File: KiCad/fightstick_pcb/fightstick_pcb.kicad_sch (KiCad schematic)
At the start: 98 parts, among them J1 USB_B_Micro, J2 Conn_01x02, J3 Conn_02x18_Odd_Even, J4 Conn_02x18_Odd_Even, SW1 SW_Push, SW10 SW_Push, SW11 SW_Push, SW12 SW_Push, SW2 SW_Push, SW3 SW_Push, SW4 SW_Push, SW5 SW_Push, SW6 SW_Push, SW7 SW_Push, SW8 SW_Push, SW9 SW_Push, U1 NCP1117-3.3_SOT223, U10 SN74LVC1G14DBV, U11 SN74LVC1G14DBV, U12 SN74LVC1G14DBV, U13 SN74LVC1G14DBV, U14 SN74LVC1G14DBV, U15 SN74LVC1G14DBV, U2 W25Q128JVS, U3 RP2040, U4 SN74LVC1G14DBV, U5 SN74LVC1G14DBV, U6 SN74LVC1G14DBV, U7 SN74LVC1G14DBV, U8 SN74LVC1G14DBV, U9 SN74LVC1G14DBV, Y1 ABM8-272-T3

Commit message: Added LEDs and Reset
Added player leds, reset button and meaningfull pin names
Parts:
- added C30: 100n, symbol Device:C
- added D2, D3, D4, D5: GREEN, symbol Device:LED
- added R31: 10k, symbol Device:R
- added R32, R33, R34, R35: 1k, symbol Device:R
- added SW13: SW_Push, symbol Switch:SW_Push
- D1: value LED -> GREEN
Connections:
- net +3V3: now also R31.1
- net GND: now also C30.2, R32.2, R33.2, R34.2, R35.2, SW13.2
- net GPIO0: no longer U3.2 (GPIO0)
- net GPIO1: no longer U3.3 (GPIO1)
- net GPIO10: no longer U3.13 (GPIO10)
- net GPIO11: no longer U3.14 (GPIO11)
- net GPIO14: no longer U9.4
- net GPIO15: no longer U10.4
- net GPIO16: no longer U11.4
- net GPIO17: no longer U7.4
- net GPIO18: no longer U13.4, U3.29 (GPIO18)
- net GPIO19: no longer U15.4, U3.30 (GPIO19)
- net GPIO2: no longer U3.4 (GPIO2)
- net GPIO20: no longer U3.31 (GPIO20), U8.4
- net GPIO21: no longer U3.32 (GPIO21), U6.4
- net GPIO22: no longer U3.34 (GPIO22), U5.4
- net GPIO23: no longer U3.35 (GPIO23), U4.4
- net GPIO24: no longer U12.4, U3.36 (GPIO24)
- net GPIO25: no longer U14.4, U3.37 (GPIO25)
- net GPIO26_ADC0: no longer RV1.2, U3.38 (GPIO26_ADC0)
- net GPIO27_ADC1: no longer RV2.2, U3.39 (GPIO27_ADC1)
- net GPIO3: no longer U3.5 (GPIO3)
- net GPIO8: no longer U3.11 (GPIO8)
- net GPIO9: no longer U3.12 (GPIO9)
- net RUN: now also C30.1, R31.2, SW13.1
- new net: D5.1 (K), R35.1
- new net: D3.1 (K), R33.1
- new net: D2.1 (K), R32.1
- new net: D4.1 (K), R34.1
- new net BUTTON_0: U10.4, U3.12 (GPIO9)
- new net BUTTON_1: U3.11 (GPIO8), U9.4
- new net BUTTON_A: U14.4, U3.37 (GPIO25)
- new net BUTTON_B: U12.4, U3.36 (GPIO24)
- new net BUTTON_LB: U13.4, U3.29 (GPIO18)
- new net BUTTON_LT: U3.34 (GPIO22), U5.4
- new net BUTTON_RB: U15.4, U3.30 (GPIO19)
- new net BUTTON_RT: U3.35 (GPIO23), U4.4
- new net BUTTON_SELECT: U11.4, U3.13 (GPIO10)
- new net BUTTON_START: U3.14 (GPIO11), U7.4
- new net BUTTON_X: U3.32 (GPIO21), U6.4
- new net BUTTON_Y: U3.31 (GPIO20), U8.4
- new net JOYSTICK_0: RV1.2, U3.38 (GPIO26_ADC0)
- new net JOYSTICK_1: RV2.2, U3.39 (GPIO27_ADC1)
- new net PLAYER_LED_0: D5.2 (A), U3.2 (GPIO0)
- new net PLAYER_LED_1: D4.2 (A), U3.3 (GPIO1)
- new net PLAYER_LED_2: D3.2 (A), U3.4 (GPIO2)
- new net PLAYER_LED_3: D2.2 (A), U3.5 (GPIO3)
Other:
- note added: "Player leds"
- note added: "Reset button"
- moved on the sheet: C17, C18, C21, C26, C27, C28, C29, J3, J4, R13, R14, R23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

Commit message: Added connectors
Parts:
- removed D2, D3, D4, D5: GREEN, symbol Device:LED
- removed J3, J4: Conn_02x18_Odd_Even, Connector_PinHeader_2.54mm:PinHeader_2x18_P2.54mm_Vertical, symbol Connector_Generic:Conn_02x18_Odd_Even
- removed RV1, RV2: R_Potentiometer, symbol Device:R_Potentiometer
- removed SW1, SW10, SW11, SW12, SW2, SW3, SW4, SW5, SW6, SW7, SW8, SW9: SW_Push, symbol Switch:SW_Push
- added J5, J6: Screw_Terminal_01x18, symbol Connector:Screw_Terminal_01x18
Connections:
- net +3V3: now also J6.18 (Pin_18)
- net GND: now also J5.1 (Pin_1), J5.11 (Pin_11), J5.13 (Pin_13), J5.15 (Pin_15), J5.17 (Pin_17), J5.3 (Pin_3), J5.5 (Pin_5), J5.7 (Pin_7), J5.9 (Pin_9), J6.1 (Pin_1), J6.12 (Pin_12), J6.14 (Pin_14), J6.16 (Pin_16)
- net SW_LB+: now reaches R25.2, R26.1
- net SW_LB+: now also J5.4 (Pin_4)
- net LED_P0-: now reaches R35.1
- net LED_P0-: now also J6.10 (Pin_10)
- net SW_0+: now reaches R19.2, R20.1
- net SW_0+: now also J6.15 (Pin_15)
- net SW_A+: now reaches R27.2, R28.1
- net SW_A+: now also J5.18 (Pin_18)
- net SW_START+: now reaches R13.2, R14.1
- net SW_START+: now also J5.2 (Pin_2)
- net SW_X+: now reaches R11.2, R12.1
- net SW_X+: now also J5.10 (Pin_10)
- net SW_B+: now reaches R23.2, R24.1
- net SW_B+: now also J5.16 (Pin_16)
- net LED_P2-: now reaches R33.1
- net LED_P2-: now also J6.6 (Pin_6)
- net SW_SELECT+: now reaches R21.2, R22.1
- net SW_SELECT+: now also J6.17 (Pin_17)
- net SW_Y+: now reaches R15.2, R16.1
- net SW_Y+: now also J5.8 (Pin_8)
- net SW_RT+: now reaches R7.2, R8.1
- net SW_RT+: now also J5.14 (Pin_14)
- net SW_1+: now reaches R17.2, R18.1
- net SW_1+: now also J6.13 (Pin_13)
- net SW_LT+: now reaches R10.1, R9.2
- net SW_LT+: now also J5.12 (Pin_12)
- net LED_P3-: now reaches R32.1
- net LED_P3-: now also J6.4 (Pin_4)
- net SW_RB+: now reaches R29.2, R30.1
- net SW_RB+: now also J5.6 (Pin_6)
- net LED_P1-: now reaches R34.1
- net LED_P1-: now also J6.8 (Pin_8)
- net BUTTON_0 renamed SIG_0
- net BUTTON_1 renamed SIG_1
- net BUTTON_A renamed SIG_A
- net BUTTON_B renamed SIG_B
- net BUTTON_LB renamed SIG_LB
- net BUTTON_LT renamed SIG_LT
- net BUTTON_RB renamed SIG_RB
- net BUTTON_RT renamed SIG_RT
- net BUTTON_SELECT renamed SIG_SELECT
- net BUTTON_START renamed SIG_START
- net BUTTON_X renamed SIG_X
- net BUTTON_Y renamed SIG_Y
- net GPIO12: no longer names the net of U3.15 (GPIO12)
- net GPIO13: no longer names the net of U3.16 (GPIO13)
- net GPIO14: no longer names the net of U3.17 (GPIO14)
- net GPIO15: no longer names the net of U3.18 (GPIO15)
- net GPIO16: no longer names the net of U3.27 (GPIO16)
- net GPIO17: no longer names the net of U3.28 (GPIO17)
- net GPIO28_ADC2: no longer names the net of U3.40 (GPIO28_ADC2)
- net GPIO29_ADC3: no longer names the net of U3.41 (GPIO29_ADC3)
- net GPIO4: no longer names the net of U3.6 (GPIO4)
- net GPIO5: no longer names the net of U3.7 (GPIO5)
- net GPIO6: no longer names the net of U3.8 (GPIO6)
- net GPIO7: no longer names the net of U3.9 (GPIO7)
- net JOYSTICK_0 renamed SIG_STICK_0
- net SIG_STICK_0: now also J6.3 (Pin_3)
- net JOYSTICK_1 renamed SIG_STICK_1
- net SIG_STICK_1: now also J6.2 (Pin_2)
- net PLAYER_LED_0 renamed LED_P0+
- net LED_P0+: now also J6.11 (Pin_11)
- net PLAYER_LED_1 renamed LED_P1+
- net LED_P1+: now also J6.9 (Pin_9)
- net PLAYER_LED_2 renamed LED_P2+
- net LED_P2+: now also J6.7 (Pin_7)
- net PLAYER_LED_3 renamed LED_P3+
- net LED_P3+: now also J6.5 (Pin_5)
- no-connect marks 1 -> 13
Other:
- note added: "Player leds (GREEN)"
- note added: "Switch terminals"
- note removed: "IOs"
- note removed: "Joystick"
- note removed: "Player leds"
- moved on the sheet: C30, C5, J2, R1, R2, R31, SW13, U2

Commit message: Updated power symbols
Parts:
- added J3: Conn_01x02, Connector_PinHeader_2.54mm:PinHeader_1x02_P2.54mm_Vertical, symbol Connector_Generic:Conn_01x02
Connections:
- net SWCLK: no longer names the net of U3.24 (SWCLK)
- net SWCLK: now also J3.1 (Pin_1)
- net SWD: no longer names the net of U3.25 (SWD)
- net SWD: now also J3.2 (Pin_2)

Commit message: New terminals
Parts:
- removed J5, J6: Screw_Terminal_01x18, symbol Connector:Screw_Terminal_01x18
- added J4, J5, J6: Screw_Terminal_01x12, symbol Connector:Screw_Terminal_01x12
- renumbered C2 to C1, C6 to C10, C7 to C11, C8 to C12, C19 to C13, C25 to C14, C9 to C15, C10 to C16, C11 to C17, C21 to C19, C3 to C2, C12 to C20, C17 to C21, C13 to C22, C14 to C23, C15 to C24, C16 to C25, C22 to C3, C23 to C4, C1 to C5, C4 to C6, C20 to C7, C24 to C8, C5 to C9, R15 to R1, R12 to R10, R20 to R11, R6 to R12, R9 to R13, R21 to R14, R10 to R15, R22 to R16, R7 to R17, R13 to R18, R8 to R19, R17 to R2, R14 to R20, R3 to R21, R4 to R22, R35 to R23, R23 to R24, R34 to R26, R24 to R27, R26 to R28, R33 to R29, R16 to R3, R32 to R30, R27 to R31, R29 to R32, R28 to R33, R30 to R34, R31 to R35, R18 to R4, R1 to R5, R2 to R6, R5 to R7, R11 to R8, R19 to R9, SW13 to SW1, U8 to U1, U4 to U10, U7 to U11, U9 to U2, U1 to U3, U2 to U4, U6 to U5, U10 to U6, U5 to U7, U11 to U8, U3 to U9
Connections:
- net +3V3: now also J6.12 (Pin_12)
- net GND: now also J5.1 (Pin_1), J5.10 (Pin_10), J5.11 (Pin_11), J5.12 (Pin_12), J5.2 (Pin_2), J5.3 (Pin_3), J5.4 (Pin_4), J5.5 (Pin_5), J5.6 (Pin_6), J5.7 (Pin_7), J5.8 (Pin_8), J5.9 (Pin_9), J6.1 (Pin_1)
- net LED_P0+: now also J6.11 (Pin_11)
- net LED_P0-: now also J6.10 (Pin_10)
- net LED_P1+: now also J6.9 (Pin_9)
- net LED_P1-: now also J6.8 (Pin_8)
- net LED_P2+: now also J6.7 (Pin_7)
- net LED_P2-: now also J6.6 (Pin_6)
- net LED_P3+: now also J6.5 (Pin_5)
- net LED_P3-: now also J6.4 (Pin_4)
- net SIG_STICK_0: now also J6.3 (Pin_3)
- net SIG_STICK_1: now also J6.2 (Pin_2)
- net SW_0+ renamed SW_0
- net SW_0: now also J4.2 (Pin_2)
- net SW_1+ renamed SW_1
- net SW_1: now also J4.1 (Pin_1)
- net SW_A+ renamed SW_A
- net SW_A: now also J4.12 (Pin_12)
- net SW_B+ renamed SW_B
- net SW_B: now also J4.11 (Pin_11)
- net SW_LB+ renamed SW_LB
- net SW_LB: now also J4.5 (Pin_5)
- net SW_LT+ renamed SW_LT
- net SW_LT: now also J4.9 (Pin_9)
- net SW_RB+ renamed SW_RB
- net SW_RB: now also J4.6 (Pin_6)
- net SW_RT+ renamed SW_RT
- net SW_RT: now also J4.10 (Pin_10)
- net SW_SELECT+ renamed SW_SELECT
- net SW_SELECT: now also J4.3 (Pin_3)
- net SW_START+ renamed SW_START
- net SW_START: now also J4.4 (Pin_4)
- net SW_X+ renamed SW_X
- net SW_X: now also J4.8 (Pin_8)
- net SW_Y+ renamed SW_Y
- net SW_Y: now also J4.7 (Pin_7)
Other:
- moved on the sheet: C1, C2, C30, C5, C6, C9, D1, J1, J2, R12, R23, R26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

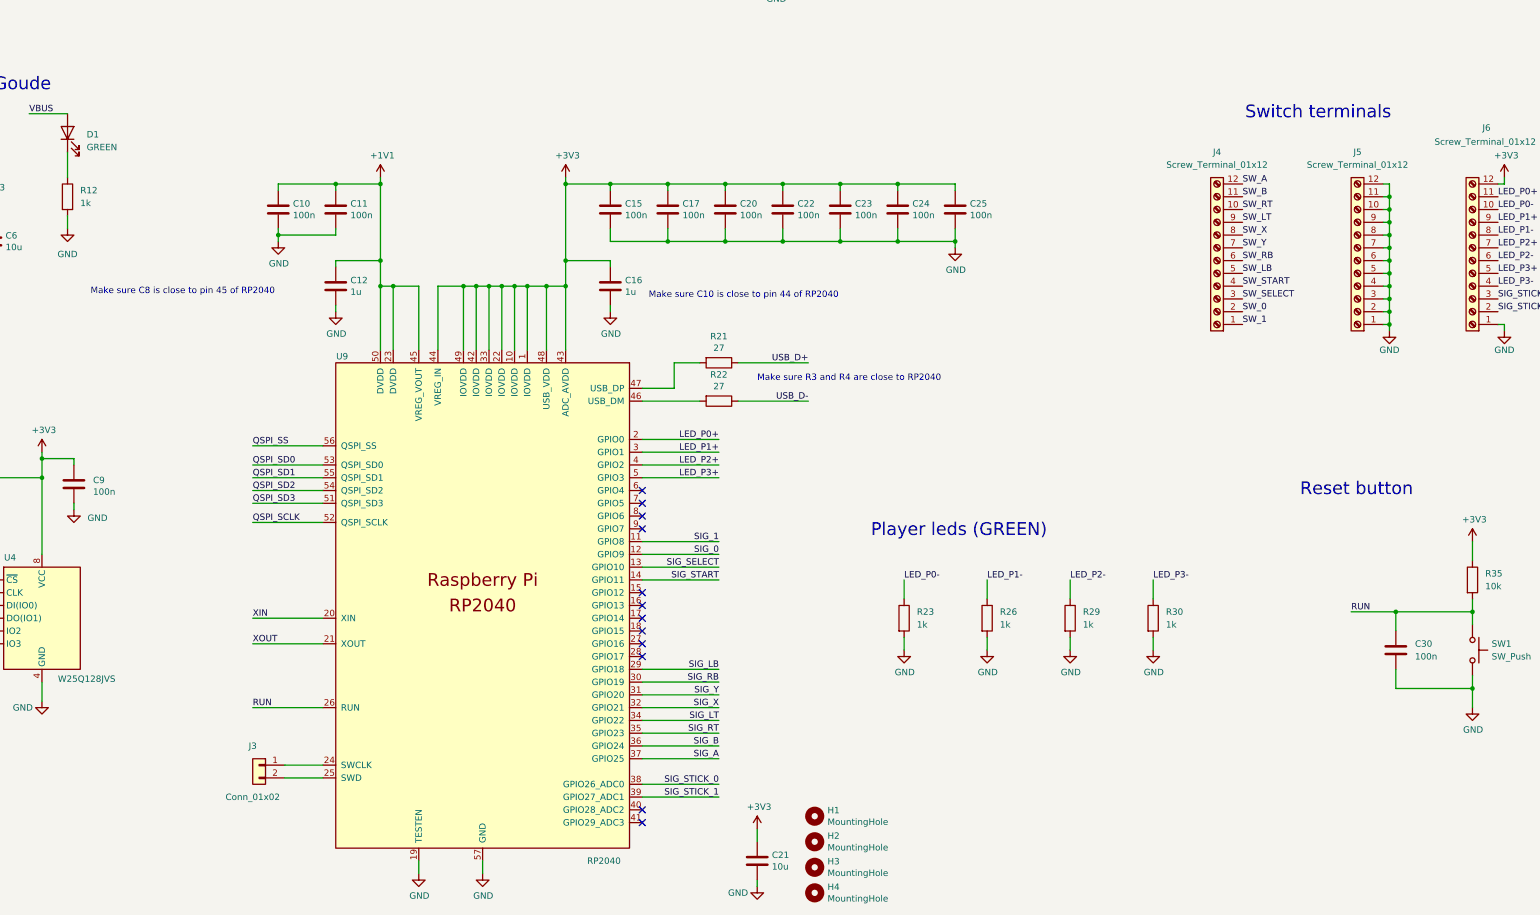
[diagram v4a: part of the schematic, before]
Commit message: Recreation of minimal design
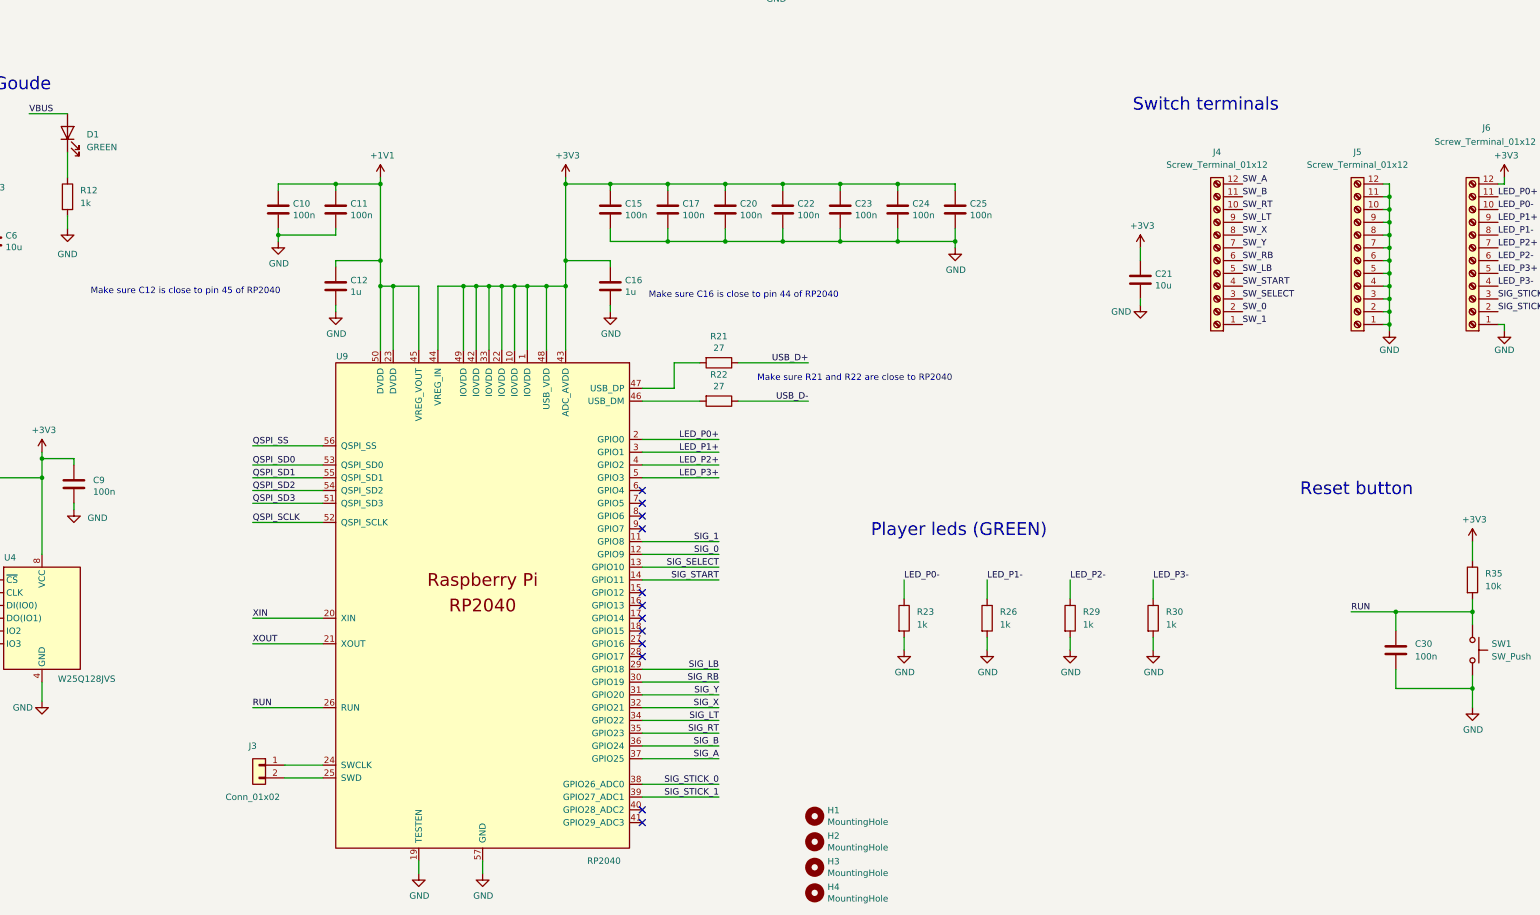
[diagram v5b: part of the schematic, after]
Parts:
- C13, C14, C18, C19, C26, C27, C28, C29, C3, C4, C7, C8: footprint (none) -> Capacitor_SMD:CP_Elec_4x3
- C30: footprint (none) -> Capacitor_SMD:C_0402_1005Metric
- D1: footprint (none) -> LED_SMD:LED_0201_0603Metric
- J4, J5, J6: footprint (none) -> TerminalBlock_4Ucon:TerminalBlock_4Ucon_1x12_P3.50mm_Horizontal
- R1, R10, R11, R12, R13, R14, R15, R16, R17, R18, R19, R2, R20, R23, R24, R25, R26, R27, R28, R29, R3, R30, R31, R32, R33, R34, R4, R8, R9: footprint (none) -> Resistor_SMD:R_0402_1005Metric
- R35: footprint (none) -> Resistor_SMD:R_0201_0603Metric_Pad0.64x0.40mm_HandSolder
- SW1: footprint (none) -> Button_Switch_SMD:SW_Push_1P1T_NO_6x6mm_H9.5mm
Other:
- note added: "Make sure C12 is close to pin 45 of RP2040"
- note added: "Make sure C16 is close to pin 44 of RP2040"
- note added: "Make sure R21 and R22 are close to RP2040"
- note removed: "Make sure C10 is close to pin 44 of RP2040"
- note removed: "Make sure C8 is close to pin 45 of RP2040"
- note removed: "Make sure R3 and R4 are close to RP2040"
- moved on the sheet: C21

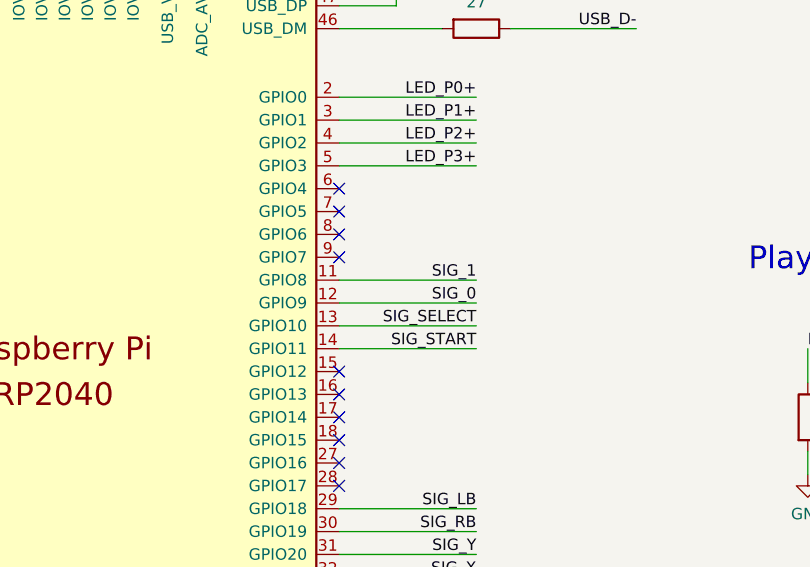
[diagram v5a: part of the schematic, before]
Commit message: Les circuits de debounce sont settés
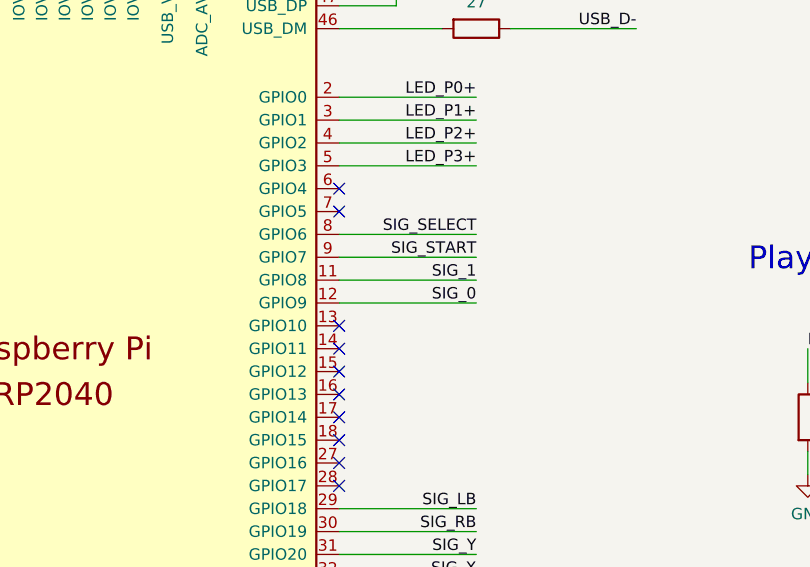
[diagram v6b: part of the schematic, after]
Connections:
- net SIG_SELECT: now also U9.8 (GPIO6); no longer U9.13 (GPIO10)
- net SIG_START: now also U9.9 (GPIO7); no longer U9.14 (GPIO11)
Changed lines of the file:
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@@
 	)
 	(no_connect
-		(at 217.17 199.39)
+		(at 217.17 212.09)
 	)
 	(no_connect
@@
 	)
 	(no_connect
+		(at 217.17 209.55)
+	)
+	(no_connect
 		(at 217.17 227.33)
 	)
@@
 	)
 	(no_connect
-		(at 217.17 201.93)
-	)
-	(no_connect
 		(at 217.17 219.71)
 	)
@@
 	(wire
 		(pts
-			(xy 217.17 209.55) (xy 232.41 209.55)
-		)
-		(stroke
-			(width 0)
-			(type default)
-		)
-	)
-	(wire
-		(pts
 			(xy 144.78 143.51) (xy 156.21 143.51)
 		)
@@
 	(wire
 		(pts
+			(xy 217.17 201.93) (xy 232.41 201.93)
+		)
+		(stroke
+			(width 0)
+			(type default)
+		)
+	)
+	(wire
+		(pts
 			(xy 166.37 77.47) (xy 167.64 77.47)
 		)
@@
 	(wire
 		(pts
+			(xy 217.17 199.39) (xy 232.41 199.39)
+		)
+		(stroke
+			(width 0)
+			(type default)
+		)
+	)
+	(wire
+		(pts
 			(xy 364.49 153.67) (xy 365.76 153.67)
 		)
@@
 	(wire
 		(pts
-			(xy 217.17 212.09) (xy 232.41 212.09)
-		)
-		(stroke
-			(width 0)
-			(type default)
-		)
-	)
-	(wire
-		(pts
 			(xy 382.27 204.47) (xy 382.27 208.28)
 		)
@@
 		)
 	)
+	(label "SIG_SELECT"
+		(at 232.41 199.39 180)
+		(fields_autoplaced yes)
+		(effects
+			(font
+				(size 1.27 1.27)
+			)
+			(justify right bottom)
+		)
+	)
 	(label "SW_0"
 		(at 87.63 82.55 0)
@@
 		)
 	)
-	(label "SIG_START"
-		(at 232.41 212.09 180)
-		(fields_autoplaced yes)
-		(effects
-			(font
-				(size 1.27 1.27)
-			)
-			(justify right bottom)
-		)
-	)
 	(label "SW_X"
 		(at 336.55 143.51 0)
@@
 		)
 	)
-	(label "SIG_SELECT"
-		(at 232.41 209.55 180)
-		(fields_autoplaced yes)
-		(effects
-			(font
-				(size 1.27 1.27)
-			)
-			(justify right bottom)
-		)
-	)
 	(label "SIG_RT"
 		(at 232.41 242.57 180)
@@
 		)
 	)
+	(label "SIG_START"
+		(at 232.41 201.93 180)
+		(fields_autoplaced yes)
+		(effects
+			(font
+				(size 1.27 1.27)
+			)
+			(justify right bottom)
+		)
+	)

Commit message: PCB Fightstick V1
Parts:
- C30: footprint Capacitor_SMD:C_0402_1005Metric -> Capacitor_SMD:C_0805_2012Metric
- D1: footprint LED_SMD:LED_0201_0603Metric -> LED_SMD:LED_0805_2012Metric
- R1, R10, R11, R12, R13, R14, R15, R16, R17, R18, R19, R2, R20, R23, R24, R25, R26, R27, R28, R29, R3, R30, R31, R32, R33, R34, R4, R8, R9: footprint Resistor_SMD:R_0402_1005Metric -> Resistor_SMD:R_0805_2012Metric
- R35: footprint Resistor_SMD:R_0201_0603Metric_Pad0.64x0.40mm_HandSolder -> Resistor_SMD:R_0805_2012Metric
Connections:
- net LED_P0+: now also J4.6 (Pin_6), U9.5 (GPIO3); no longer J6.11 (Pin_11), U9.2 (GPIO0)
- net LED_P0-: now also J4.5 (Pin_5); no longer J6.10 (Pin_10)
- net LED_P1+: now also J4.10 (Pin_10), U9.6 (GPIO4); no longer J6.9 (Pin_9), U9.3 (GPIO1)
- net LED_P1-: now also J4.9 (Pin_9); no longer J6.8 (Pin_8)
- net LED_P2+: now also J6.5 (Pin_5), U9.7 (GPIO5); no longer J6.7 (Pin_7), U9.4 (GPIO2)
- net LED_P2-: now also J6.4 (Pin_4); no longer J6.6 (Pin_6)
- net LED_P3+: now also J6.9 (Pin_9), U9.8 (GPIO6); no longer J6.5 (Pin_5), U9.5 (GPIO3)
- net LED_P3-: now also J6.8 (Pin_8); no longer J6.4 (Pin_4)
- net SIG_0: now also U9.13 (GPIO10); no longer U9.12 (GPIO9)
- net SIG_1: now also U9.12 (GPIO9); no longer U9.11 (GPIO8)
- net SIG_LB: now also U9.4 (GPIO2); no longer U9.29 (GPIO18)
- net SIG_RB: now also U9.3 (GPIO1); no longer U9.30 (GPIO19)
- net SIG_SELECT: now also U9.9 (GPIO7); no longer U9.8 (GPIO6)
- net SIG_START: now also U9.11 (GPIO8); no longer U9.9 (GPIO7)
- net SIG_STICK_0: now also J4.1 (Pin_1); no longer J6.3 (Pin_3)
- net SIG_STICK_1: now also J4.2 (Pin_2); no longer J6.2 (Pin_2)
- net SW_0: now also J6.11 (Pin_11); no longer J4.2 (Pin_2)
- net SW_1: now also J6.10 (Pin_10); no longer J4.1 (Pin_1)
- net SW_LB: now also J6.3 (Pin_3); no longer J4.5 (Pin_5)
- net SW_LT: now also J4.7 (Pin_7); no longer J4.9 (Pin_9)
- net SW_RB: now also J6.2 (Pin_2); no longer J4.6 (Pin_6)
- net SW_RT: now also J4.8 (Pin_8); no longer J4.10 (Pin_10)
- net SW_SELECT: now also J6.6 (Pin_6); no longer J4.3 (Pin_3)
- net SW_START: now also J6.7 (Pin_7); no longer J4.4 (Pin_4)
- net SW_X: now also J4.4 (Pin_4); no longer J4.8 (Pin_8)
- net SW_Y: now also J4.3 (Pin_3); no longer J4.7 (Pin_7)
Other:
- moved on the sheet: J6
